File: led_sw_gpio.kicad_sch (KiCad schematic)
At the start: 0 parts

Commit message: Add components: TXS0108E, FT232 oscillators/power/USB, symbol library table
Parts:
- added R10, R11, R12, R13, R14, R15: 2k2, Resistor_SMD:R_0805_2012Metric, symbol Device:R
- added SW1: power, Button_Switch_SMD:SW_SPST_CK_RS282G05A3, symbol Switch:SW_DIP_x01
- added SW2: up, Button_Switch_SMD:SW_SPST_CK_RS282G05A3, symbol Switch:SW_DIP_x01
- added SW3: down, Button_Switch_SMD:SW_SPST_CK_RS282G05A3, symbol Switch:SW_DIP_x01
- added SW4: left, Button_Switch_SMD:SW_SPST_CK_RS282G05A3, symbol Switch:SW_DIP_x01
- added SW5: rigth, Button_Switch_SMD:SW_SPST_CK_RS282G05A3, symbol Switch:SW_DIP_x01
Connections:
- new net: R12.2, SW1.1
- new net +12V: R12.1
- new net +3.3V: R10.1, R11.1, R14.1, R15.1
- new net GND: R13.2, SW2.2, SW3.2, SW4.2, SW5.2
- new net RD4: R11.2, SW2.1
- new net RD5: R10.2, SW3.1
- new net RD6: R15.2, SW4.1
- new net RD7: R14.2, SW5.1
- new net SW_PWR: R13.1, SW1.2

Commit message: ESP32S3 branch initial changes
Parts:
- removed R12, R13: 2k2, Resistor_SMD:R_0805_2012Metric, symbol Device:R
- added D3, D4, D5, D6: LED, Diode_SMD:D_0805_2012Metric, symbol Device:LED
- added R1, R2, R3, R4, R5, R6, R7, R8: 2k2, Resistor_SMD:R_0805_2012Metric, symbol Device:R
- added SW2: down, Button_Switch_SMD:SW_Push_1P1T_NO_CK_KSC9xxG, symbol Switch:SW_DIP_x01
- added SW3: left, Button_Switch_SMD:SW_Push_1P1T_NO_CK_KSC9xxG, symbol Switch:SW_DIP_x01
- added SW4: rigth, Button_Switch_SMD:SW_Push_1P1T_NO_CK_KSC9xxG, symbol Switch:SW_DIP_x01
- SW1: value power -> up; footprint Button_Switch_SMD:SW_SPST_CK_RS282G05A3 -> Button_Switch_SMD:SW_Push_1P1T_NO_CK_KSC9xxG
- SW5: renamed from SW2; footprint Button_Switch_SMD:SW_SPST_CK_RS282G05A3 -> Button_Switch_SMD:SW_Push_1P1T_NO_CK_KSC9xxG
- SW6: renamed from SW3; footprint Button_Switch_SMD:SW_SPST_CK_RS282G05A3 -> Button_Switch_SMD:SW_Push_1P1T_NO_CK_KSC9xxG
- SW7: renamed from SW4; footprint Button_Switch_SMD:SW_SPST_CK_RS282G05A3 -> Button_Switch_SMD:SW_Push_1P1T_NO_CK_KSC9xxG
- SW8: renamed from SW5; footprint Button_Switch_SMD:SW_SPST_CK_RS282G05A3 -> Button_Switch_SMD:SW_Push_1P1T_NO_CK_KSC9xxG
- renumbered R11 to R10, R14 to R11, R15 to R12, R10 to R9
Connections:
- net SW_PWR is gone; now on net GND: SW1.2
- net GND: now also R1.1, R2.1, R3.1, R4.1, SW2.2, SW3.2, SW4.2
- net sw1: now reaches SW1.1
- net sw1: now also R6.2
- net +3.3V renamed +3V3
- net +3V3: now also D3.1 (K), D4.1 (K), D5.1 (K), D6.1 (K), R5.1, R6.1, R7.1, R8.1
- net RD4 renamed sw5
- net RD5 renamed sw6
- net RD6 renamed sw7
- net RD7 renamed sw8
- new net: D4.2 (A), R2.2
- new net: D5.2 (A), R3.2
- new net: D6.2 (A), R4.2
- new net: D3.2 (A), R1.2
- new net sw2: R5.2, SW2.1
- new net sw3: R8.2, SW3.1
- new net sw4: R7.2, SW4.1
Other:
- moved on the sheet: R10, R11, R12, R9, SW5, SW6, SW7, SW8

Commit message: ESP32S3 push before GPIO label changes
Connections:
- net +3V3: no longer D3.1 (K), D4.1 (K), D5.1 (K), D6.1 (K)
- new net led3: D3.1 (K)
- new net led4: D4.1 (K)
- new net led5: D5.1 (K)
- new net led6: D6.1 (K)
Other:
- moved on the sheet: D3, D4, D5, D6, R1, R2, R3, R4, R5, R6, SW1, SW2

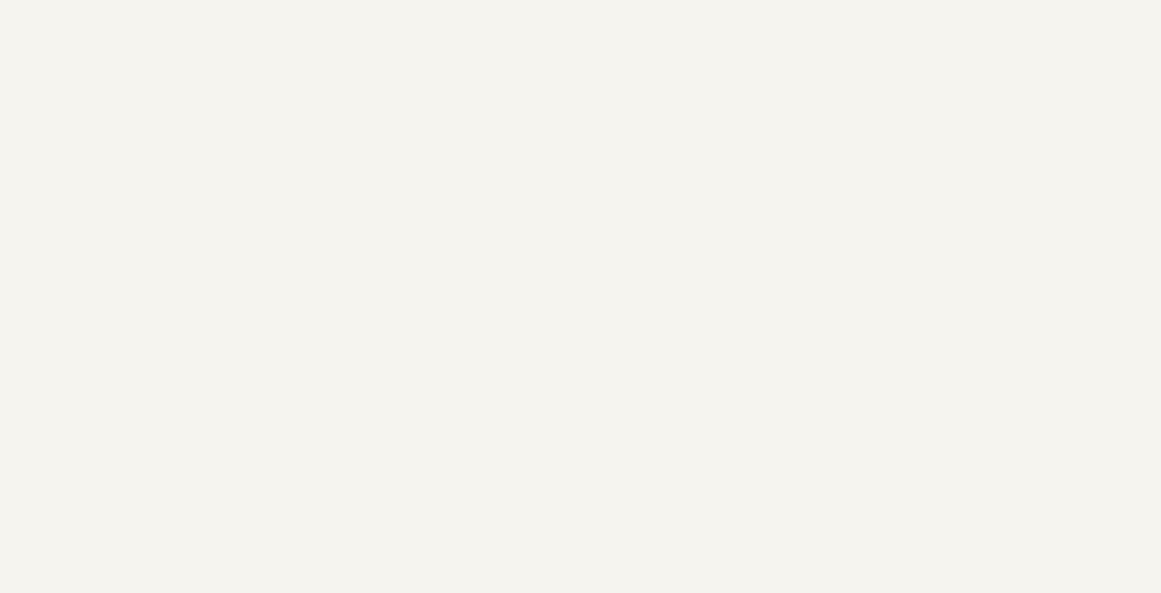
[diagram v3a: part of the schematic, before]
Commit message: ESP32S3: rename hierarchical GPIO labels and remove PCB tracks
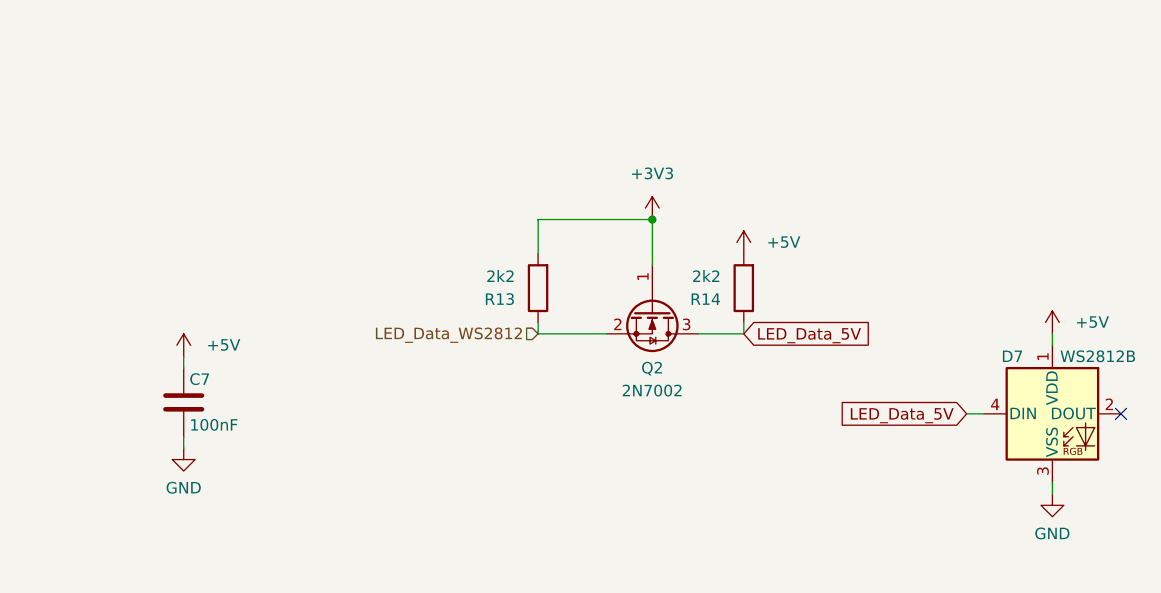
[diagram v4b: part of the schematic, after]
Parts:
- added C7: 100nF, Capacitor_SMD:C_0805_2012Metric, symbol Device:C
- added D7: WS2812B, LED_SMD:LED_WS2812B_PLCC4_5.0x5.0mm_P3.2mm, symbol LED:WS2812B
- added Q2: 2N7002, Package_TO_SOT_SMD:SOT-23, symbol Transistor_FET:2N7002
- added R13, R14: 2k2, Resistor_SMD:R_0805_2012Metric, symbol Device:R
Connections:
- net +3V3: now also Q2.1 (G), R13.2
- net GND: now also C7.2, D7.3 (VSS)
- new net +5V: C7.1, D7.1 (VDD), R14.2
- new net LED_Data_5V: D7.4 (DIN), Q2.3 (D), R14.1
- new net LED_Data_WS2812: Q2.2 (S), R13.1
- no-connect marks 0 -> 1
